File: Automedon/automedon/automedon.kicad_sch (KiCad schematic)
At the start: 12 parts, among them J1 701W-X2/03, J13 T4131012041-000, J16 T4131012041-000, J2 MS3100E24-22P, J3 PWM-02RMFS-TS7001, J4 PWM-02RMFS-TS7001, J45 PWM-02RMFS-TS7001, J5 MSXS-08PFFP-SF7002, J6 MSXS-08PFFP-SF7002, SW1 RRS20F1ABLKREDBLK31P, SW3 KEYSWITCH_SPST

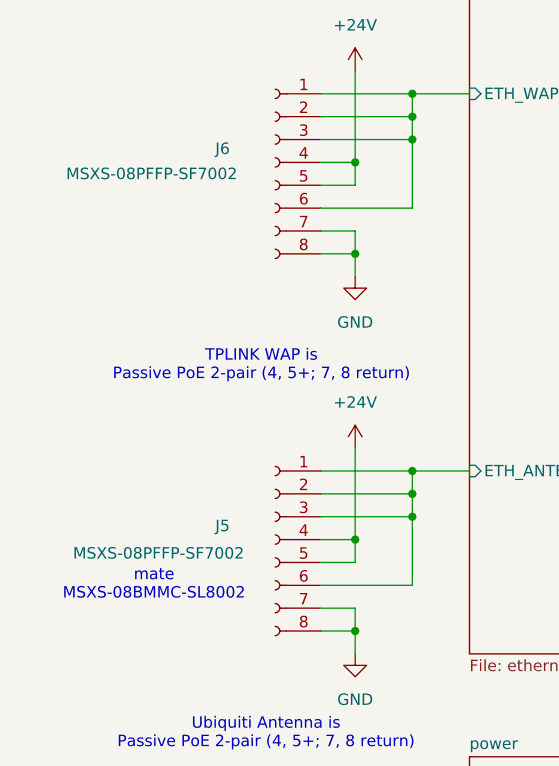
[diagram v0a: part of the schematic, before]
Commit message: Revert "Update connector"
This reverts commit 3a37b6a19b99deb2b7118eab30d8044c58bd28a2.
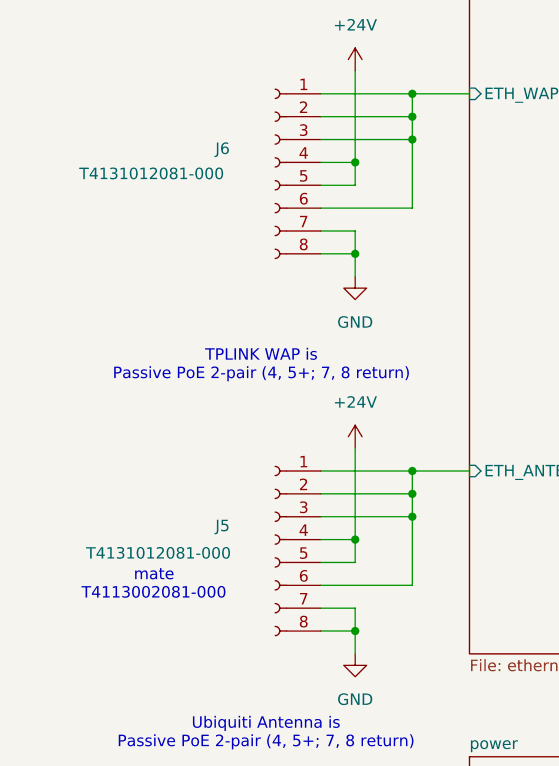
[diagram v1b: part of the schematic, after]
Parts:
- J5, J6: value MSXS-08PFFP-SF7002 -> T4131012081-000
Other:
- note added: "mate T4113002081-000"
- note removed: "mate MSXS-08BMMC-SL8002"
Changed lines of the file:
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@@
 		)
 	)
-	(text "mate\nMSXS-08BMMC-SL8002"
+	(text "mate\nT4113002081-000"
 		(exclude_from_sim no)
 		(at 27.178 270.51 0)
@@
 			)
 		)
-		(property "Value" "MSXS-08PFFP-SF7002"
+		(property "Value" "T4131012081-000"
 			(at 27.686 266.954 0)
 			(effects
@@
 			)
 		)
-		(property "Value" "MSXS-08PFFP-SF7002"
+		(property "Value" "T4131012081-000"
 			(at 26.924 224.79 0)
 			(effects

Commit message: Update a bunch of shit
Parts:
- removed J13, J16: T4131012041-000, symbol Connector:Conn_01x04_Socket
- added J57, J58: Eth Ext 4 pin, symbol Connector:Conn_01x04_Socket
- MES1: value Voltmeter Display -> Adafruit 575 Voltmeter
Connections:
- net ethernet/ETH_EXT_1: now also J57.1 (Pin_1), J57.2 (Pin_2), J57.3 (Pin_3), J57.4 (Pin_4)
- net ethernet/ETH_EXT_2: now also J58.1 (Pin_1), J58.2 (Pin_2), J58.3 (Pin_3), J58.4 (Pin_4)
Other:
- note removed: "mate T4113001041-000"
- moved on the sheet: J5, J6
